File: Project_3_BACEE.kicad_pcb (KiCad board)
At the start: 2 copper layers, 0 parts

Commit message: Set design rules.
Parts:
- added BT1: Battery 3V, Connector_PinHeader_2.54mm:PinHeader_1x02_P2.54mm_Vertical, F.Cu at (126.7, 118.4)
- added C1: 22pF, Capacitor_SMD:C_0805_2012Metric_Pad1.15x1.40mm_HandSolder, F.Cu at (175.1, 137.7)
- added C2: 22pF, Capacitor_SMD:C_0805_2012Metric_Pad1.15x1.40mm_HandSolder, F.Cu at (175.3, 143.6)
- added C3: 10uF, Capacitor_SMD:C_0805_2012Metric_Pad1.15x1.40mm_HandSolder, F.Cu at (170.6, 147.8)
- added D1: LED, LED_SMD:LED_0805_2012Metric_Pad1.15x1.40mm_HandSolder, F.Cu at (165.8, 146.8)
- added J1: Digital pins, Connector_PinSocket_2.54mm:PinSocket_1x09_P2.54mm_Vertical, F.Cu at (107.7, 118.4)
- added J2: Serial, Connector_PinSocket_2.54mm:PinSocket_1x04_P2.54mm_Vertical, F.Cu at (116.1, 118.4)
- added J3: ICSP, Connector_PinSocket_2.54mm:PinSocket_2x03_P2.54mm_Vertical, F.Cu at (122.7, 118.4)
- added J4: I2C, Connector_PinSocket_2.54mm:PinSocket_1x04_P2.54mm_Vertical, F.Cu at (112.0, 118.4)
- added R1: 330R, Resistor_SMD:R_0805_2012Metric_Pad1.15x1.40mm_HandSolder, F.Cu at (175.1, 140.6)
- added R2: 10k, Resistor_SMD:R_0805_2012Metric_Pad1.15x1.40mm_HandSolder, F.Cu at (170.6, 144.9)
- added U1: 24LC1025, Package_SO:SOIJ-8_5.3x5.3mm_P1.27mm, F.Cu at (162.8, 141.8)
- added U2: 24LC1025, Package_SO:SOIJ-8_5.3x5.3mm_P1.27mm, F.Cu at (162.8, 134.8)
- added U3: DS1337S+, Package_SO:SO-8_5.3x6.2mm_P1.27mm, F.Cu at (151.4, 146.7)
- added U4: ATMEGA328P-AU, digikey-footprints:TQFP-32_7x7mm, F.Cu at (151.8, 137.1)
- added Y1: Crystal 32 MHz, Crystal:Crystal_SMD_MicroCrystal_CC7V-T1A-2Pin_3.2x1.5mm_HandSoldering, F.Cu at (160.1, 147.0)
- added Y2: Crystal 16 MHz, Crystal:Crystal_SMD_5032-2Pin_5.0x3.2mm_HandSoldering, F.Cu at (173.2, 133.8)
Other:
- net class Power added: clearance 0.2, trace_width 0.3, via_dia 1, via_drill 0.6

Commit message: Placement complete.
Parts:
- moved R2 77.1 mm to (117.7, 88.7), turned to 180 degrees
- moved C2 70.0 mm to (128.0, 91.9)
- moved Y2 66.7 mm to (120.5, 92.9)
- moved C1 63.7 mm to (128.0, 94.7)
- moved C3 53.3 mm to (144.3, 101.5)
- moved U3 51.9 mm to (148.1, 94.9)
- moved U2 47.0 mm to (136.5, 95.9)
- moved Y1 46.5 mm to (149.5, 101.7)
- moved R1 46.3 mm to (144.3, 106.1)
- moved U1 46.2 mm to (136.5, 103.8)
- moved U4 43.6 mm to (125.3, 102.4)
- moved D1 43.6 mm to (150.1, 106.2)
- moved J4 40.3 mm to (138.4, 87.9), turned to 90 degrees
- moved J2 31.5 mm to (124.0, 87.9), turned to 90 degrees
- moved BT1 29.4 mm to (112.9, 92.5)
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
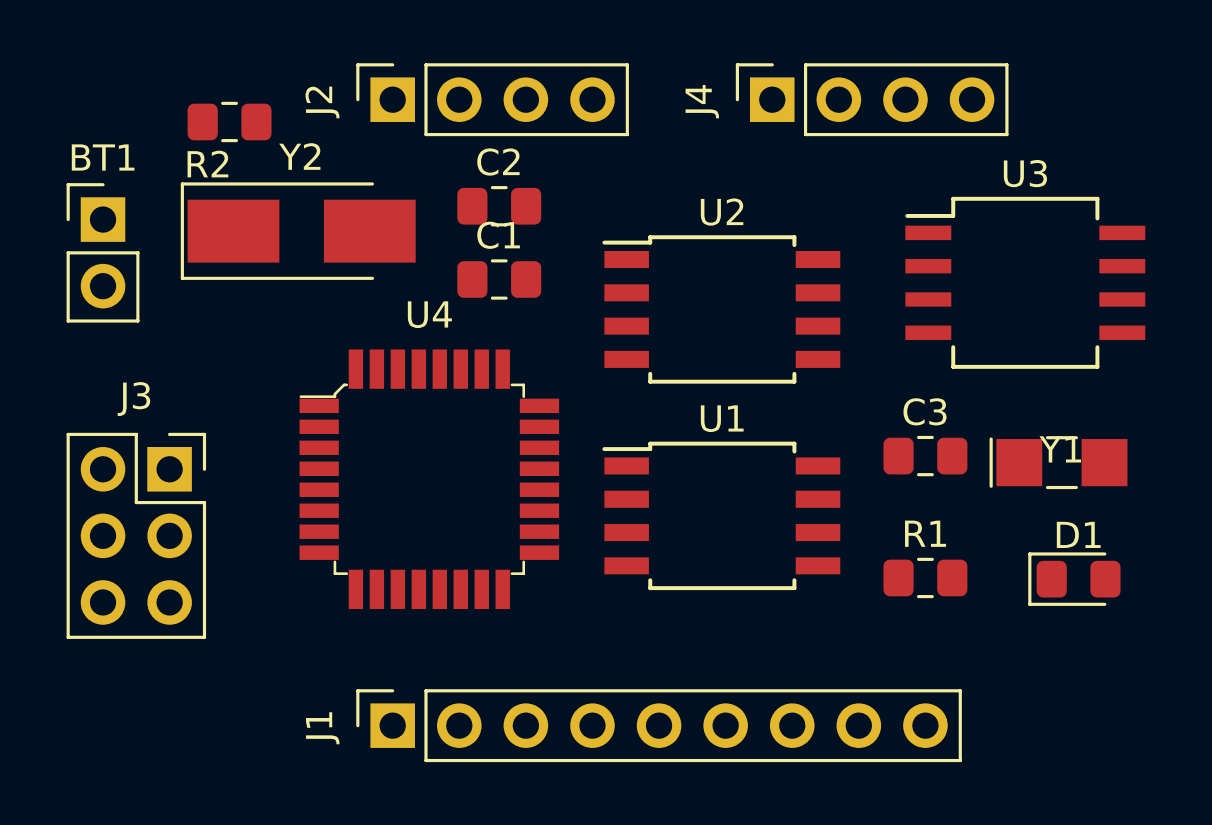
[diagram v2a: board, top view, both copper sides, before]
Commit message: Created outline and mounting holes.
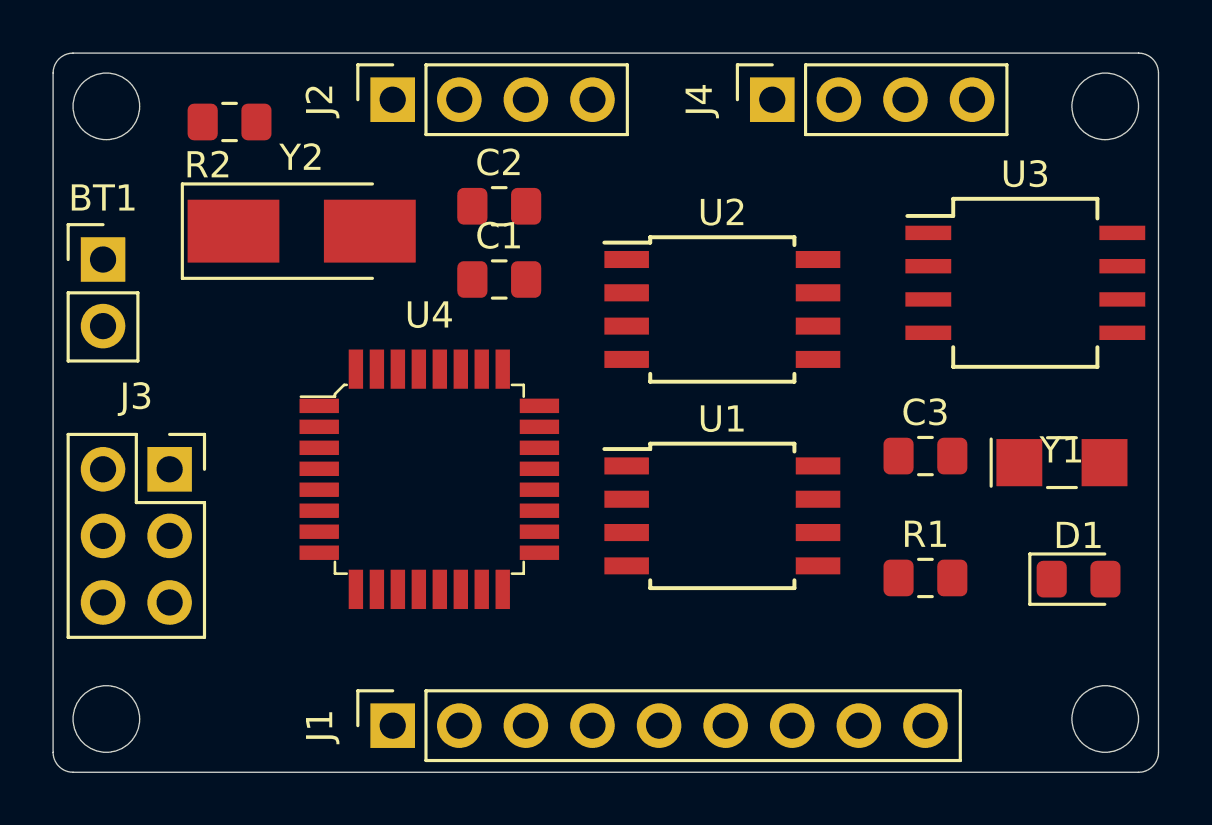
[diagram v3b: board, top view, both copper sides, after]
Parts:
- moved BT1 1.52 mm to (112.9, 94.0)
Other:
- board outline added: 42.2 x 27.4 mm
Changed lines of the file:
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@@
   (general
     (thickness 1.6)
-    (drawings 0)
+    (drawings 12)
     (tracks 0)
     (zones 0)
@@
   )
   (module Connector_PinHeader_2.54mm:PinHeader_1x02_P2.54mm_Vertical (layer F.Cu)
-    (at 112.903 92.456)
+    (at 112.903 93.98)
     (descr "Through hole straight pin header, 1x02, 2.54mm pitch, single row")
     (tags "Through hole pin header THT 1x02 2.54mm single row")
@@
     )
   )
+  (gr_circle (center 151.13 88.138) (end 149.86 88.138) (layer Edge.Cuts) (width 0.05))
+  (gr_circle (center 151.13 111.506) (end 149.86 111.506) (layer Edge.Cuts) (width 0.05))
+  (gr_circle (center 113.03 111.506) (end 111.76 111.506) (layer Edge.Cuts) (width 0.05))
+  (gr_circle (center 113.03 88.138) (end 111.76 88.138) (layer Edge.Cuts) (width 0.05))
+  (gr_line (start 153.162 112.776) (end 153.162 86.868) (layer Edge.Cuts) (width 0.05))
+  (gr_line (start 111.76 113.538) (end 152.4 113.538) (layer Edge.Cuts) (width 0.05))
+  (gr_line (start 152.4 86.106) (end 111.76 86.106) (layer Edge.Cuts) (width 0.05))
+  (gr_line (start 110.998 112.776) (end 110.998 86.868) (layer Edge.Cuts) (width 0.05))
+  (gr_arc (start 152.4 86.868) (end 153.162 86.868) (angle -90) (layer Edge.Cuts) (width 0.05))
+  (gr_arc (start 152.4 112.776) (end 152.4 113.538) (angle -90) (layer Edge.Cuts) (width 0.05))
+  (gr_arc (start 111.76 112.776) (end 110.998 112.776) (angle -90) (layer Edge.Cuts) (width 0.05))
+  (gr_arc (start 111.76 86.868) (end 111.76 86.106) (angle -90) (layer Edge.Cuts) (width 0.05))
 )
